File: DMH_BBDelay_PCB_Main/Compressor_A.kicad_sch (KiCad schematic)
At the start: 23 parts, among them U24 SSI2162, U25 TL074

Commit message: Added notes from troubleshooting
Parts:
- C84: now not fitted
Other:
- note added: "Bypassing this capacitor improved the frequent loud excursions of this compressor. I suspect it's because the input current is relatively large: a +5Vp will give 500uA at the VCA input. If the input signal for any reason tops at 11V (max OpAmp output), the current will be 1.1mA, still within the headroom of 2mA input current of the VCA. Nevertheless, try higher input resistor values here while re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"
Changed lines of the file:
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@@
 		(comment 1 "PCB for 10cm Kosmo format synthesizer module")
+	)
+	(text "Bypassing this capacitor improved the frequent loud excursions\nof this compressor. I suspect it's because the input current is\nrelatively large: a +5Vp will give 500uA at the VCA input.\nIf the input signal for any reason tops at 11V (max OpAmp output),\nthe current will be 1.1mA, still within the headroom of 2mA\ninput current of the VCA.\nNevertheless, try higher input resistor values here while restoring the\n2.2nF capacitor."
+		(exclude_from_sim no)
+		(at 99.822 137.668 0)
+		(effects
+			(font
+				(size 1.27 1.27)
+			)
+		)
 	)
 	(junction
@@
 		(on_board yes)
 		(in_pos_files yes)
-		(dnp no)
+		(dnp yes)
 		(property "Reference" "C84"
 			(at 50.8 134.62 0)

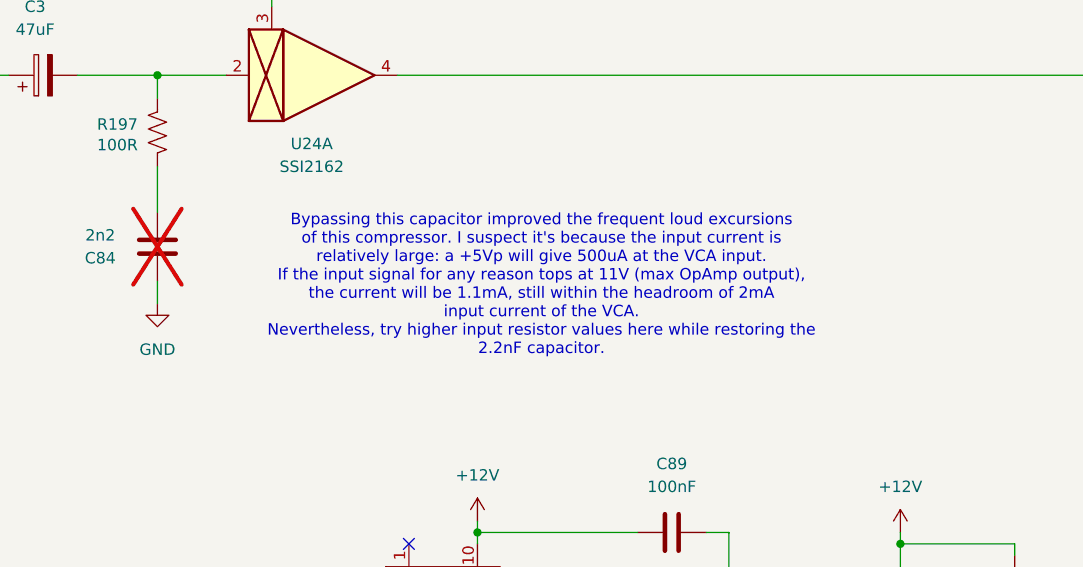
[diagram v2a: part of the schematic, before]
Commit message: Scaled up components in Tone Control part
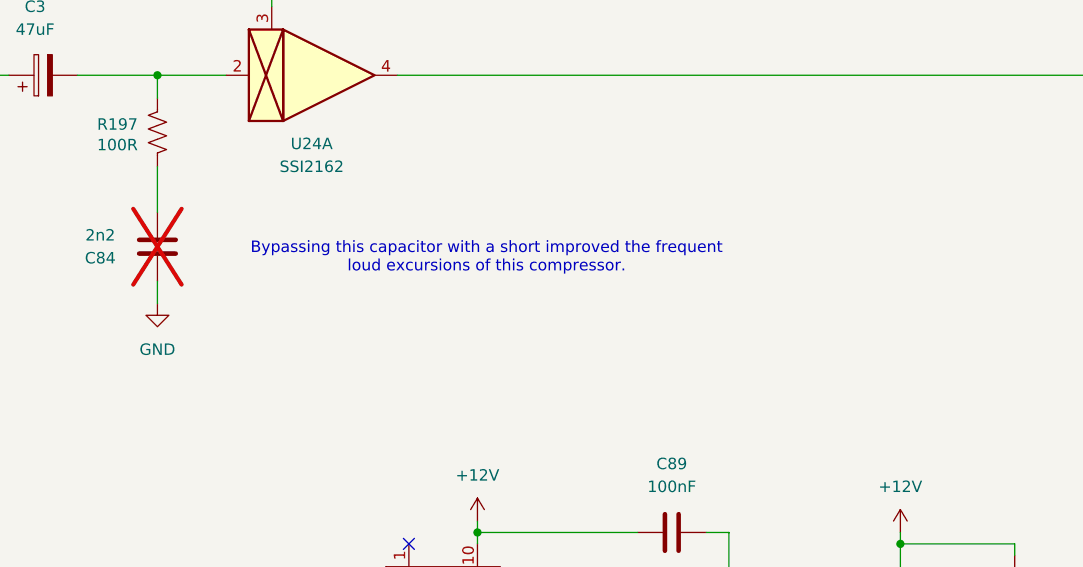
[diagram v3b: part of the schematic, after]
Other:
- note added: "Bypassing this capacitor with a short improved the frequent loud excursions of this compressor."
- note removed: "Bypassing this capacitor improved the frequent loud excursions of this compressor. I suspect it's because the input current is relatively large: a +5Vp will give 500uA at the VCA input. If the input signal for any reason tops at 11V (max OpAmp output), the current will be 1.1mA, still within the headroom of 2mA input current of the VCA. Nevertheless, try higher input resistor values here while re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"
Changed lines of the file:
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@@
 		(comment 1 "PCB for 10cm Kosmo format synthesizer module")
 	)
-	(text "Bypassing this capacitor improved the frequent loud excursions\nof this compressor. I suspect it's because the input current is\nrelatively large: a +5Vp will give 500uA at the VCA input.\nIf the input signal for any reason tops at 11V (max OpAmp output),\nthe current will be 1.1mA, still within the headroom of 2mA\ninput current of the VCA.\nNevertheless, try higher input resistor values here while restoring the\n2.2nF capacitor."
+	(text "Bypassing this capacitor with a short improved the frequent\nloud excursions of this compressor."
 		(exclude_from_sim no)
-		(at 99.822 137.668 0)
+		(at 93.726 134.62 0)
 		(effects
 			(font

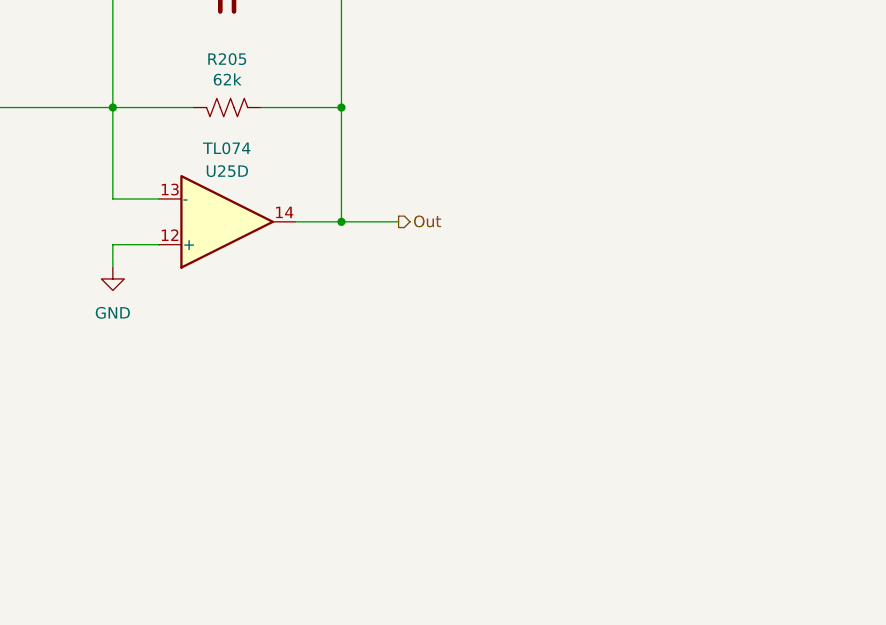
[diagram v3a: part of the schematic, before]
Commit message: Added clamping to compressors outputs
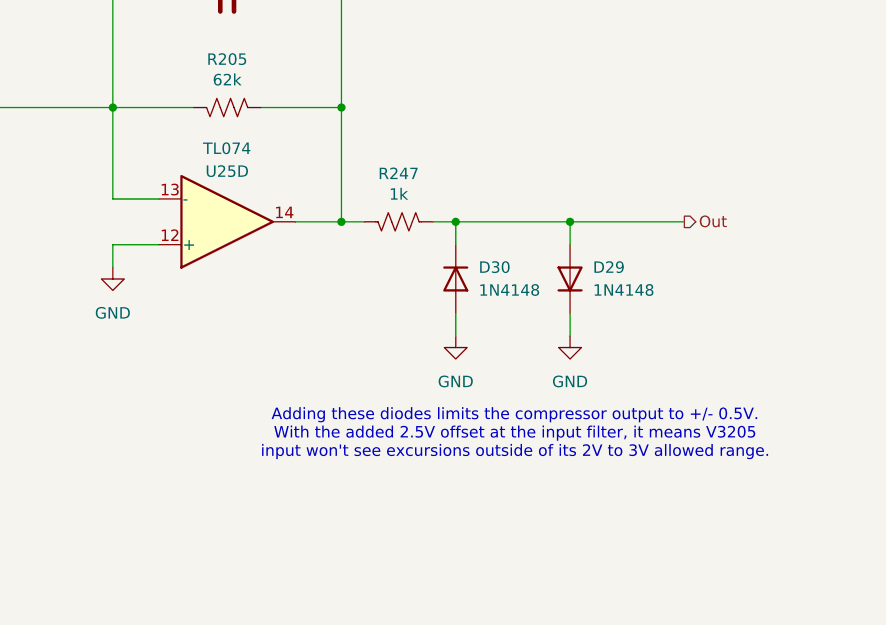
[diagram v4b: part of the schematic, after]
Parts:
- added D29, D30: 1N4148, Diode_THT:D_DO-35_SOD27_P7.62mm_Horizontal, symbol Diode:1N4148
- added R247: 1k, Resistor_THT:R_Axial_DIN0207_L6.3mm_D2.5mm_P7.62mm_Horizontal, symbol Device:R_US
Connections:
- net GND: now also D29.1 (K), D30.2 (A)
- net Out: now also D29.2 (A), D30.1 (K), R247.2; no longer C86.2, R204.1, R205.2, U25.14
- new net: C86.2, R204.1, R205.2, R247.1, U25.14
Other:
- note added: "Adding these diodes limits the compressor output to +/- 0.5V. With the added 2.5V offset at the input filter, it means V3205 input won't see excursions outside of its 2V to 3V allowed range."
